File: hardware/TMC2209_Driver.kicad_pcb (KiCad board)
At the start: 2 copper layers, 36.7 x 39.4 mm, 27 parts, among them J1 PCIe_Stepper, J2 Conn_01x04_Male, U1 TMC2209-LA, U2 74LVC1G06

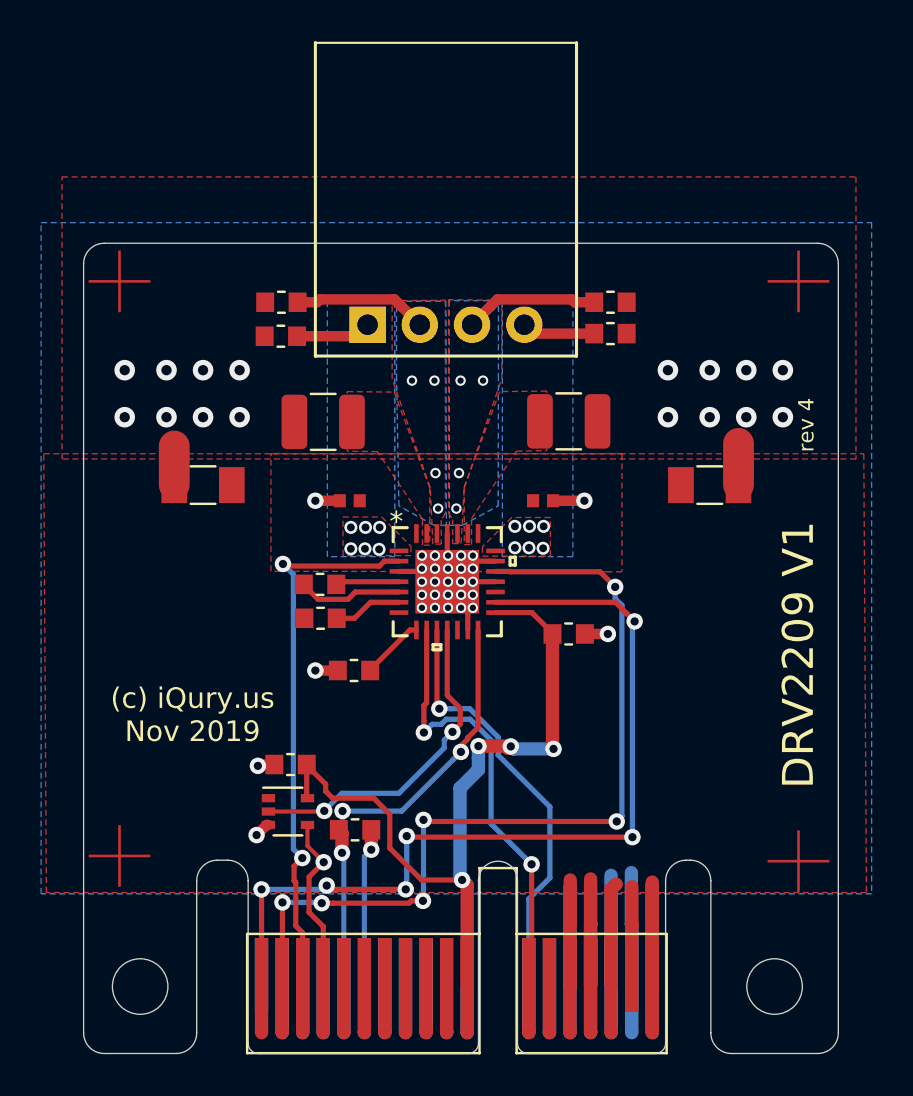
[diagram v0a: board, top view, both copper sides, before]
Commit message: Add I2C EEPROM to the 2209 driver board for identification.
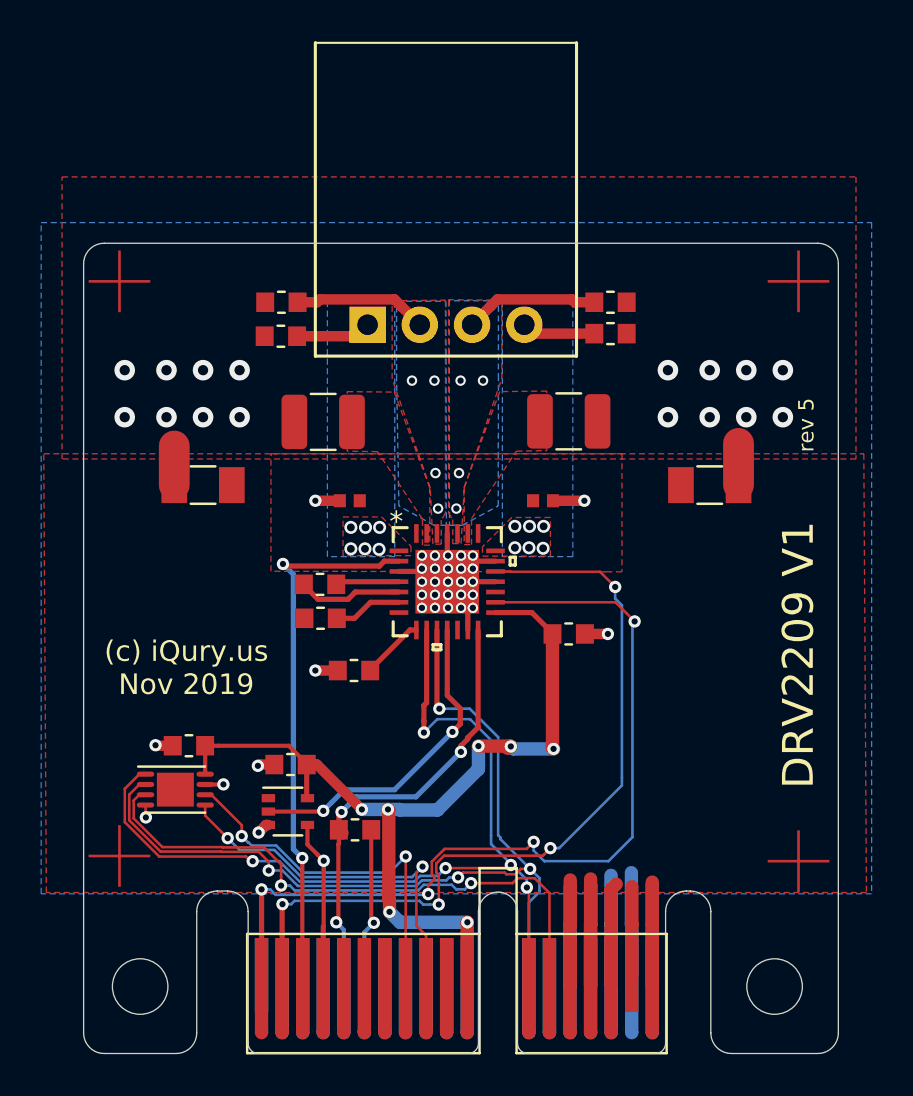
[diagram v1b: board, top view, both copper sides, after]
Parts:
- added C14: 0.1uF, PrntrBoardV2:C_0603_1608Metric, F.Cu at (114.1, 99.0)
- added U3: 24LC02, Package_DFN_QFN:TDFN-8-1EP_3x2mm_P0.5mm_EP1.80x1.65mm, F.Cu at (113.5, 101.2)
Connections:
- J1 pad B13: (no net) -> /ID_2
- J1 pad B8: (no net) -> /SCL
- J1 pad B9: (no net) -> /SDA
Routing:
- net /ID_2: track 0.00 -> 29.1 mm, vias 0 -> 2
- net /ID_1: track 20.8 -> 44.2 mm, vias 1 -> 4
- net /ID_0: track 21.8 -> 45.1 mm, vias 2 -> 5
- net /SDA: track 0.00 -> 18.6 mm, vias 0 -> 2
- net /SCL: track 0.00 -> 18.2 mm, vias 0 -> 2
- net VCC: track 37.6 -> 44.4 mm, vias 4 -> 7
- net GND: track 46.6 -> 48.8 mm, vias 47 -> 50
- net /DIR: track 42.1 -> 40.3 mm, vias 6 -> 4
- net /ALARM1: track 8.74 -> 8.19 mm
- net /STEP: track 43.1 -> 43.6 mm, vias 6 -> 4
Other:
- outline, holes or cut-outs redrawn
- board text added: "rev 5"
- board text removed: "rev 4"

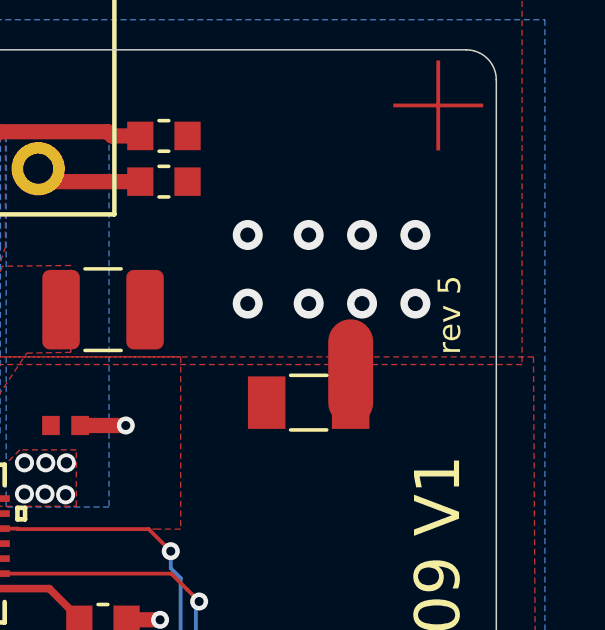
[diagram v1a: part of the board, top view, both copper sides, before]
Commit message: The 2209 driver is still rev 4.
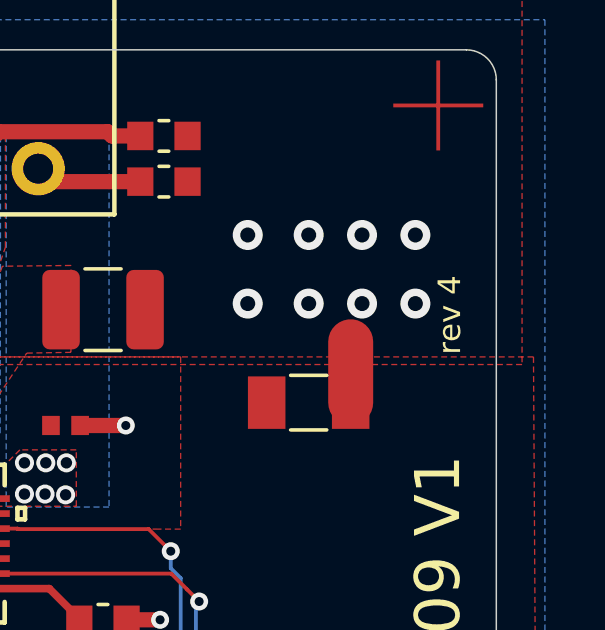
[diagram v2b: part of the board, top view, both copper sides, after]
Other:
- board text added: "rev 4"
- board text removed: "rev 5"

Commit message: Update drv2209 to rev 5.
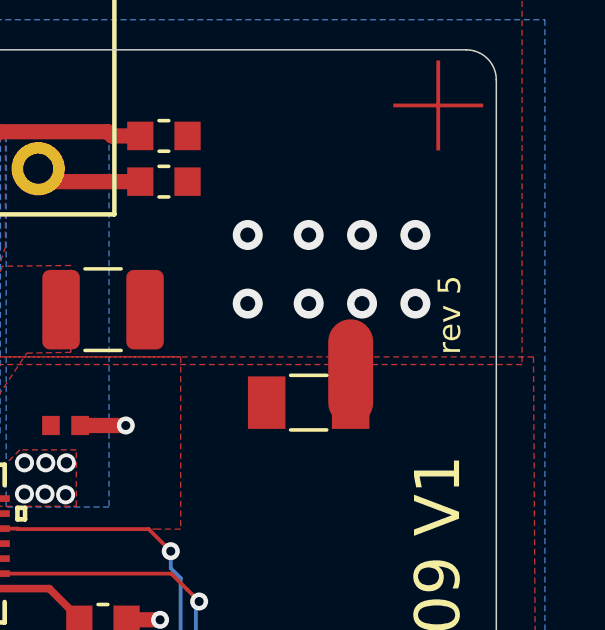
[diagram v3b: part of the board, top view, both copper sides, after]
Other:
- board text added: "rev 5"
- board text removed: "rev 4"

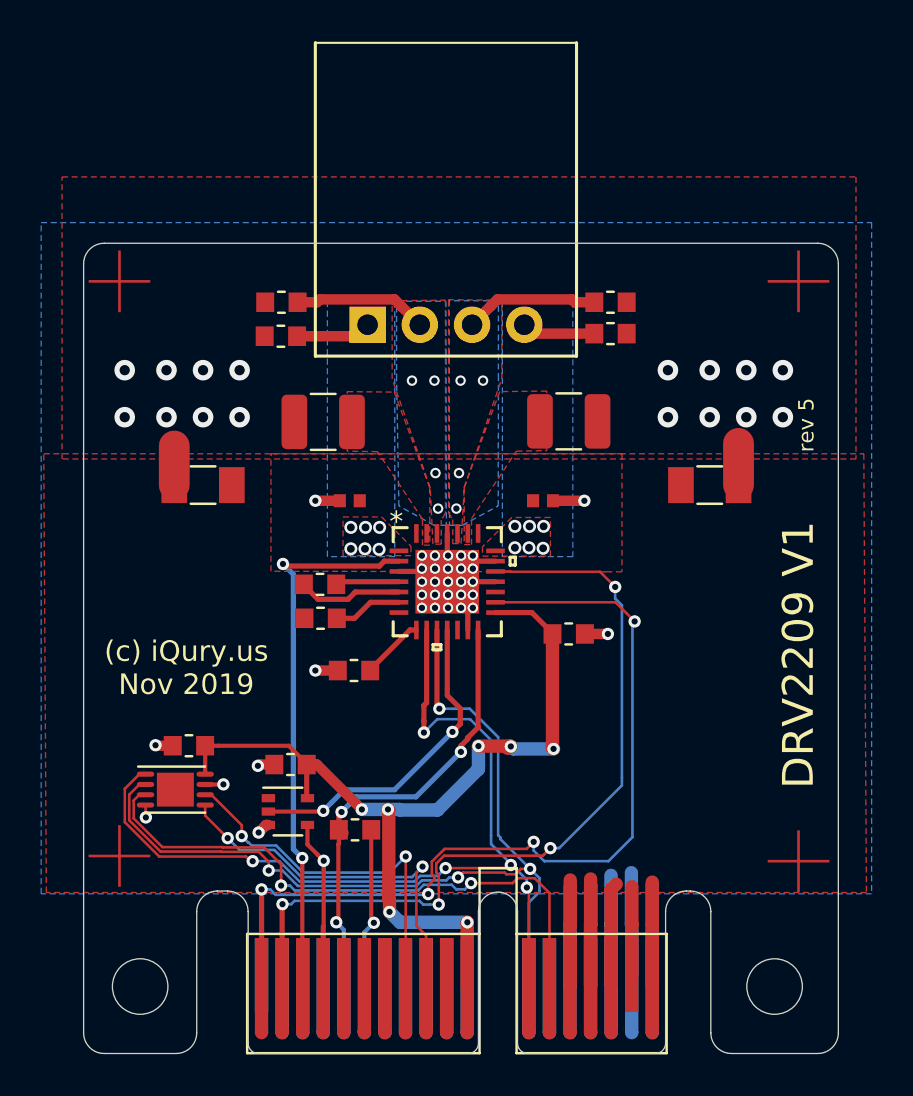
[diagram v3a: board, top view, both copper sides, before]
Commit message: Remove some vias on the 2209 driver.
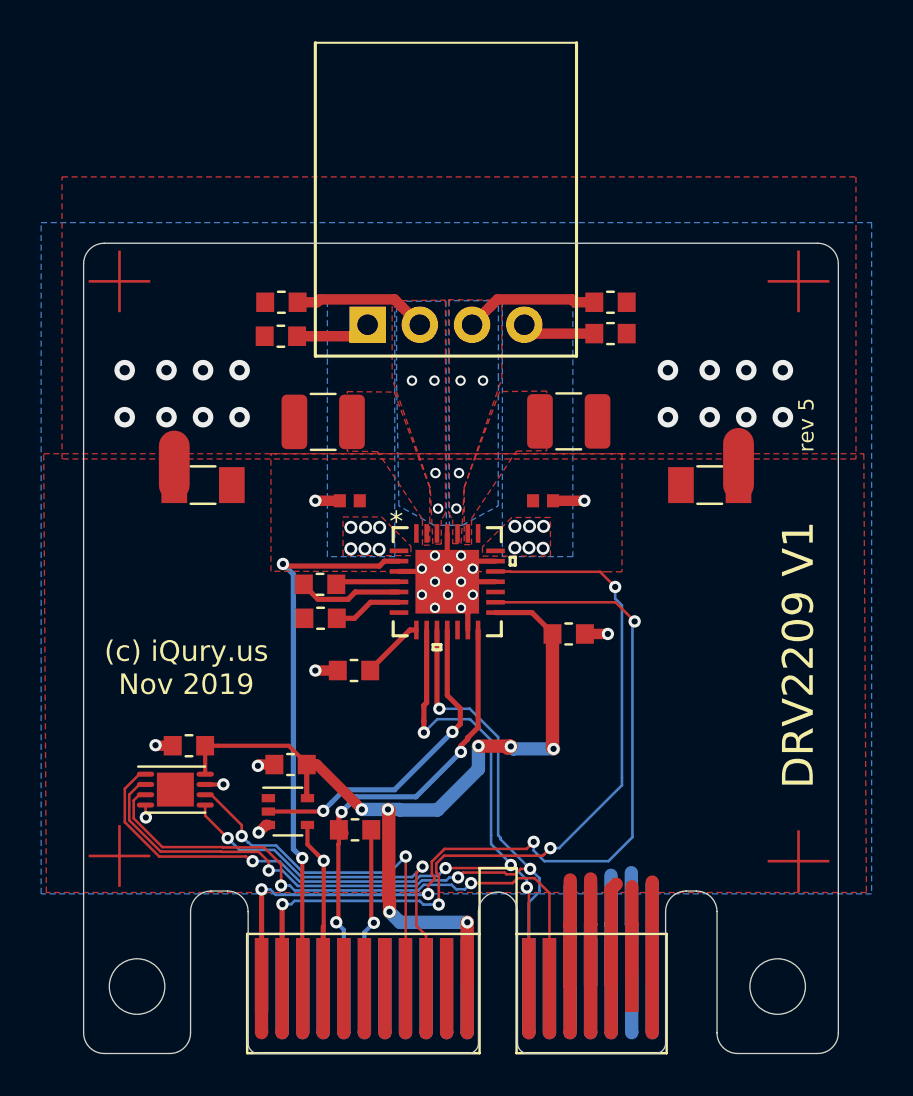
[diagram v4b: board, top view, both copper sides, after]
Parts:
- moved H1 0.15 mm to (111.6, 110.7)
- moved H2 0.15 mm to (142.8, 110.7)
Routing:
- net GND: vias 50 -> 37
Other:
- outline, holes or cut-outs redrawn

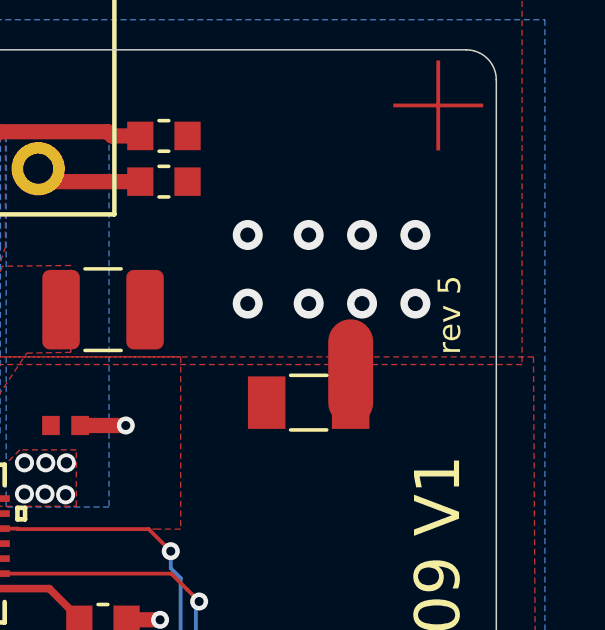
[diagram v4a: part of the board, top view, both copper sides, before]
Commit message: Update 2209 rev to 6.
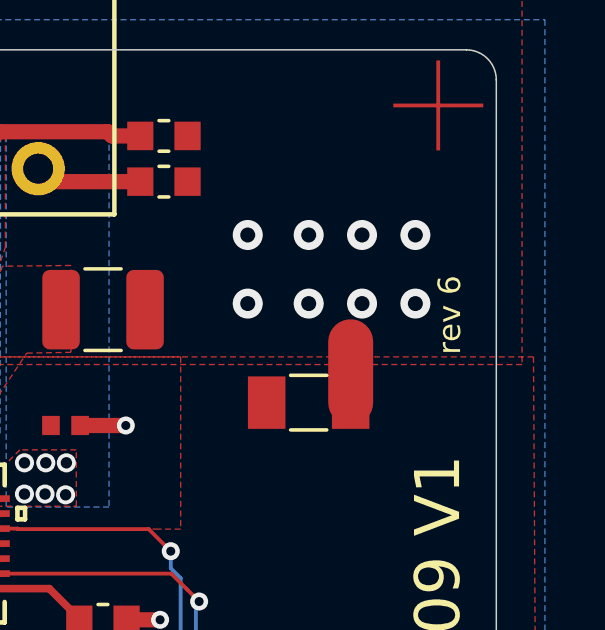
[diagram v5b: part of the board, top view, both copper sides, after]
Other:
- board text added: "rev 6"
- board text removed: "rev 5"
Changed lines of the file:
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@@
     (effects (font (size 1 1) (thickness 0.15)))
   )
-  (gr_text "rev 5" (at 144.145 83.439 90) (layer "F.SilkS")
+  (gr_text "rev 6" (at 144.145 83.439 90) (layer "F.SilkS")
     (effects (font (size 0.75 0.75) (thickness 0.1)))
   )

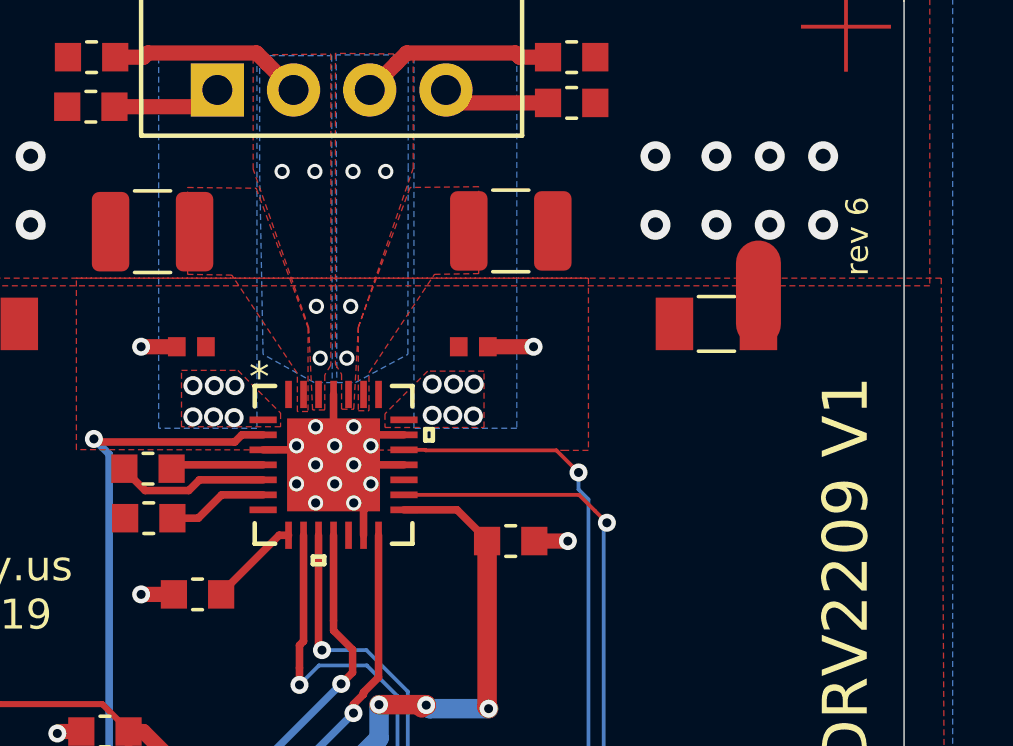
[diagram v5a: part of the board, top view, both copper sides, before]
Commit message: Update QFN footprint to match the Trinamic spec.
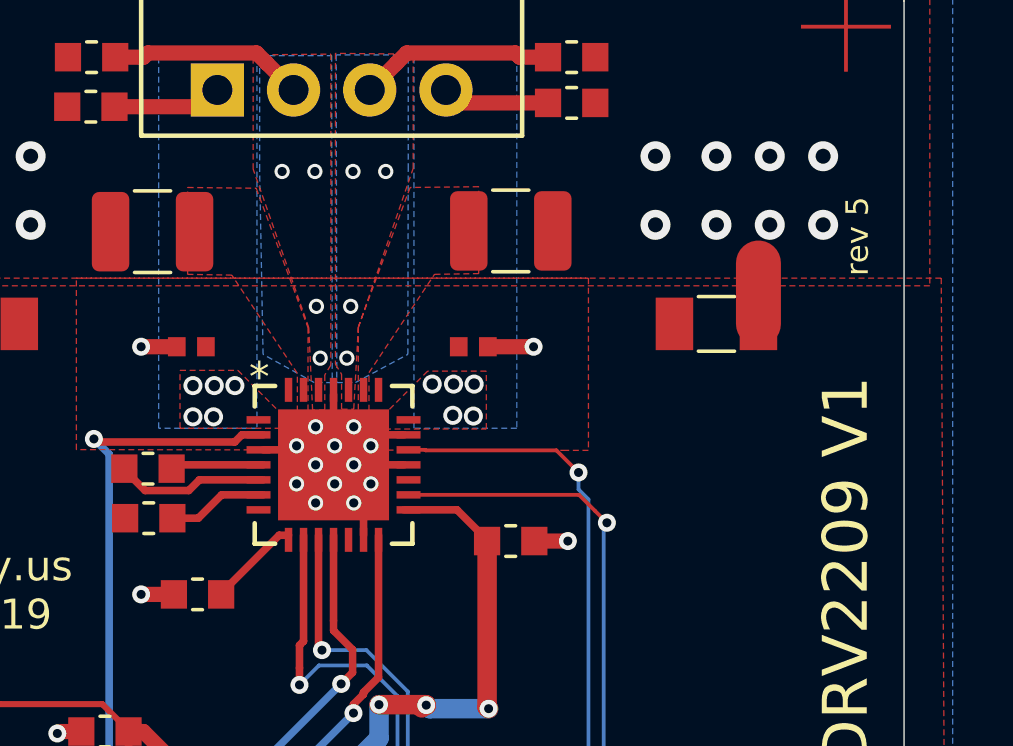
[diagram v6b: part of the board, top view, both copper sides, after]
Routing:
- net /MOTB2: vias 6 -> 5
- net /MOTA2: vias 6 -> 5
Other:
- board text added: "rev 5"
- board text removed: "rev 6"

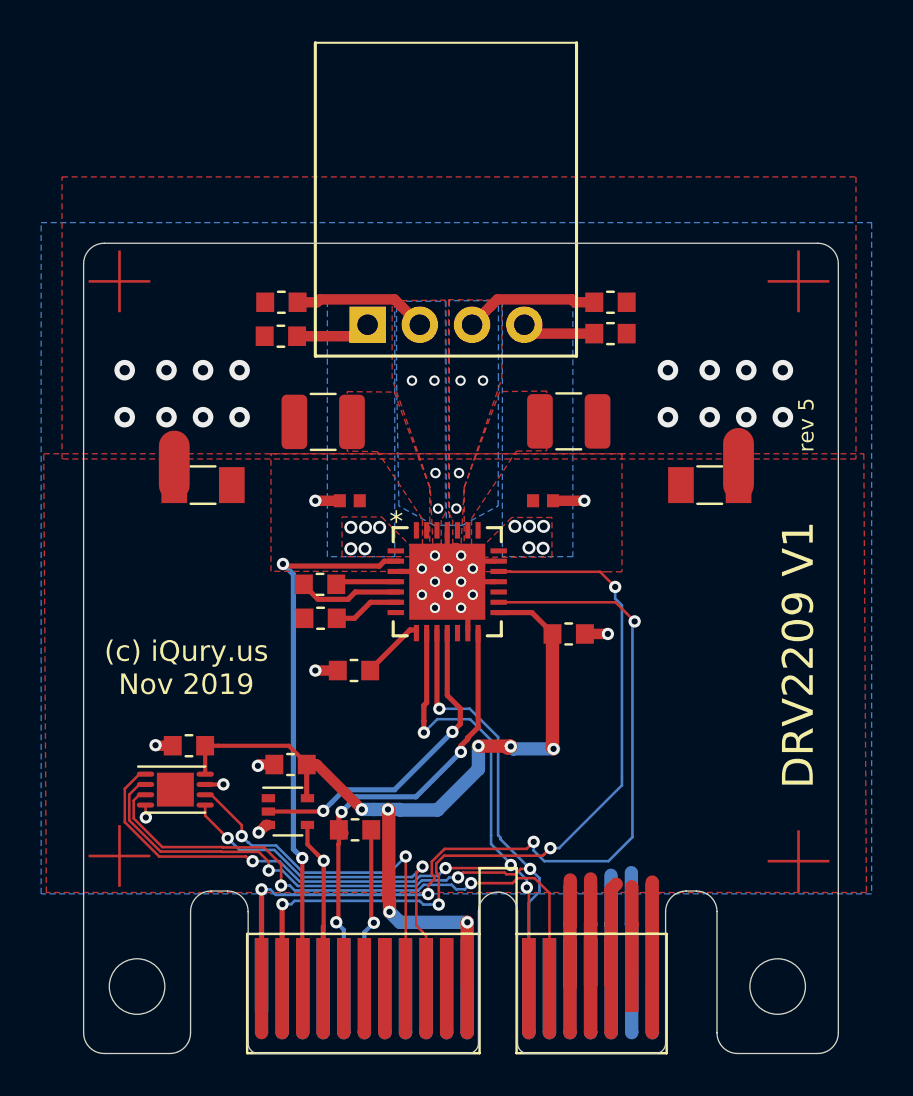
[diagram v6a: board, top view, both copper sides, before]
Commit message: Fix design rules for the 2208 driver. Update EEPROM foorprint.
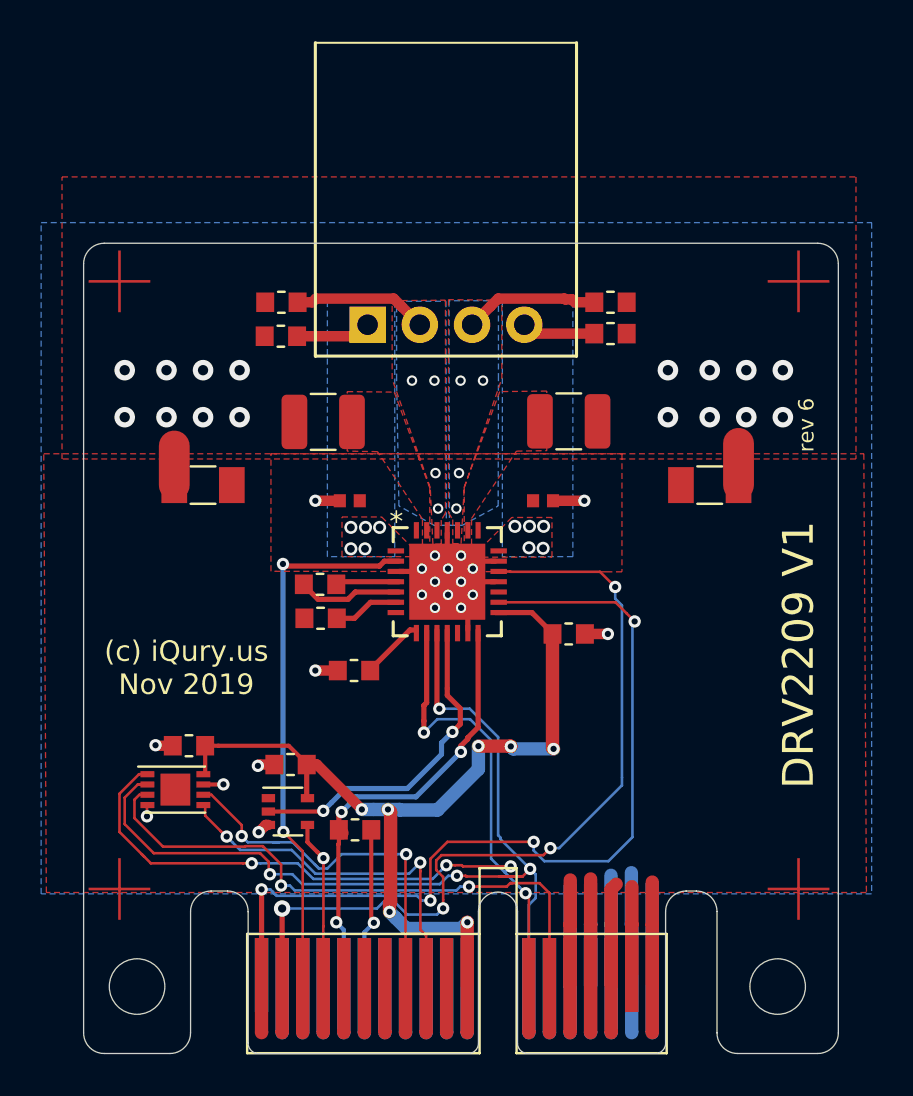
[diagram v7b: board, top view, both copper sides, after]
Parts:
- U3: footprint Package_DFN_QFN:TDFN-8-1EP_3x2mm_P0.5mm_EP1.80x1.65mm -> PrntrBoardV2:TDFN-8-1EP_3x2mm_P0.5mm_EP1.56x1.45mm
- moved FID4 1.61 mm to (110.7, 106.0)
- moved FID2 1.35 mm to (143.8, 106.0)
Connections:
- J1 pad : (no net) -> /~ENABLE
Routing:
- net /ID_1: track 44.2 -> 45.9 mm
- net /ID_0: track 45.1 -> 46.4 mm
- net /DIR: track 40.3 -> 41.1 mm
- net /STEP: track 43.6 -> 44.3 mm
- net /SCL: track 18.2 -> 18.8 mm
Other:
- net class Default: clearance 0.0889 -> 0.127
- rule trace_clearance: 0.0889 -> 0.127
- rule trace_min: 0.0889 -> 0.127
- board text added: "rev 6"
- board text removed: "rev 5"
